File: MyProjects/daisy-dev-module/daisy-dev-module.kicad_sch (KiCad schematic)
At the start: 28 parts, among them J13 Gate_1, J14 Gate_2, J17 Gate_OUT_1, J18 Gate_OUT_2, Q1 MMBT3904, Q2 MMBT3904, U8 TL074

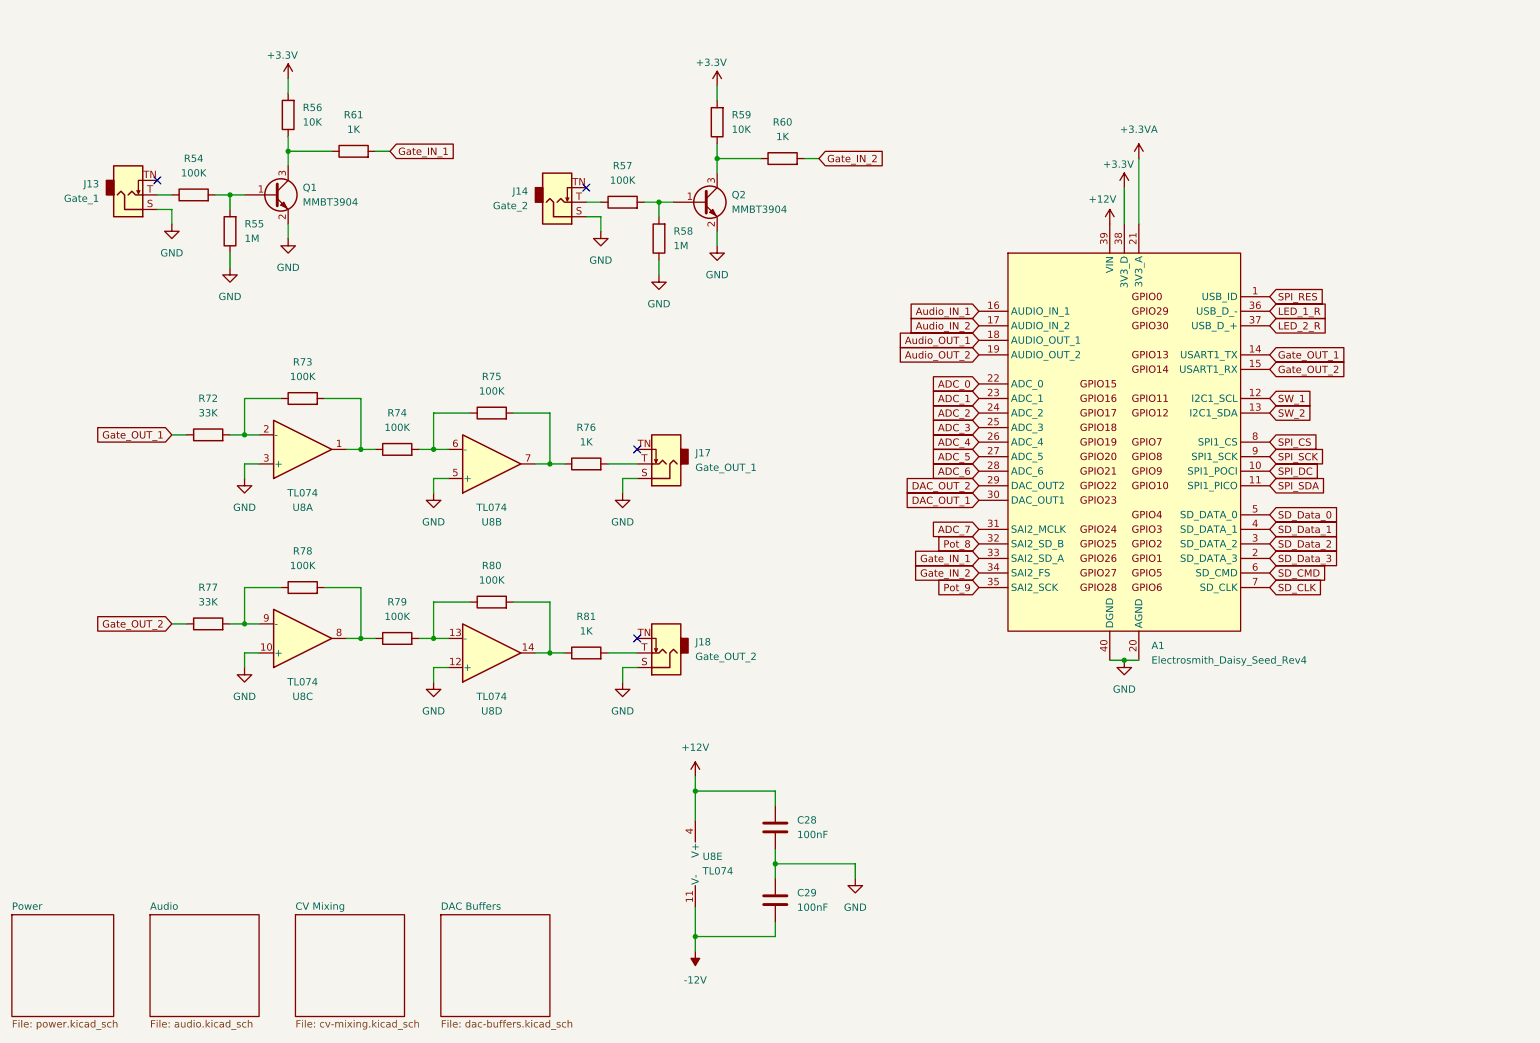
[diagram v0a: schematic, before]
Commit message: Create daisy-dev-module-test repo
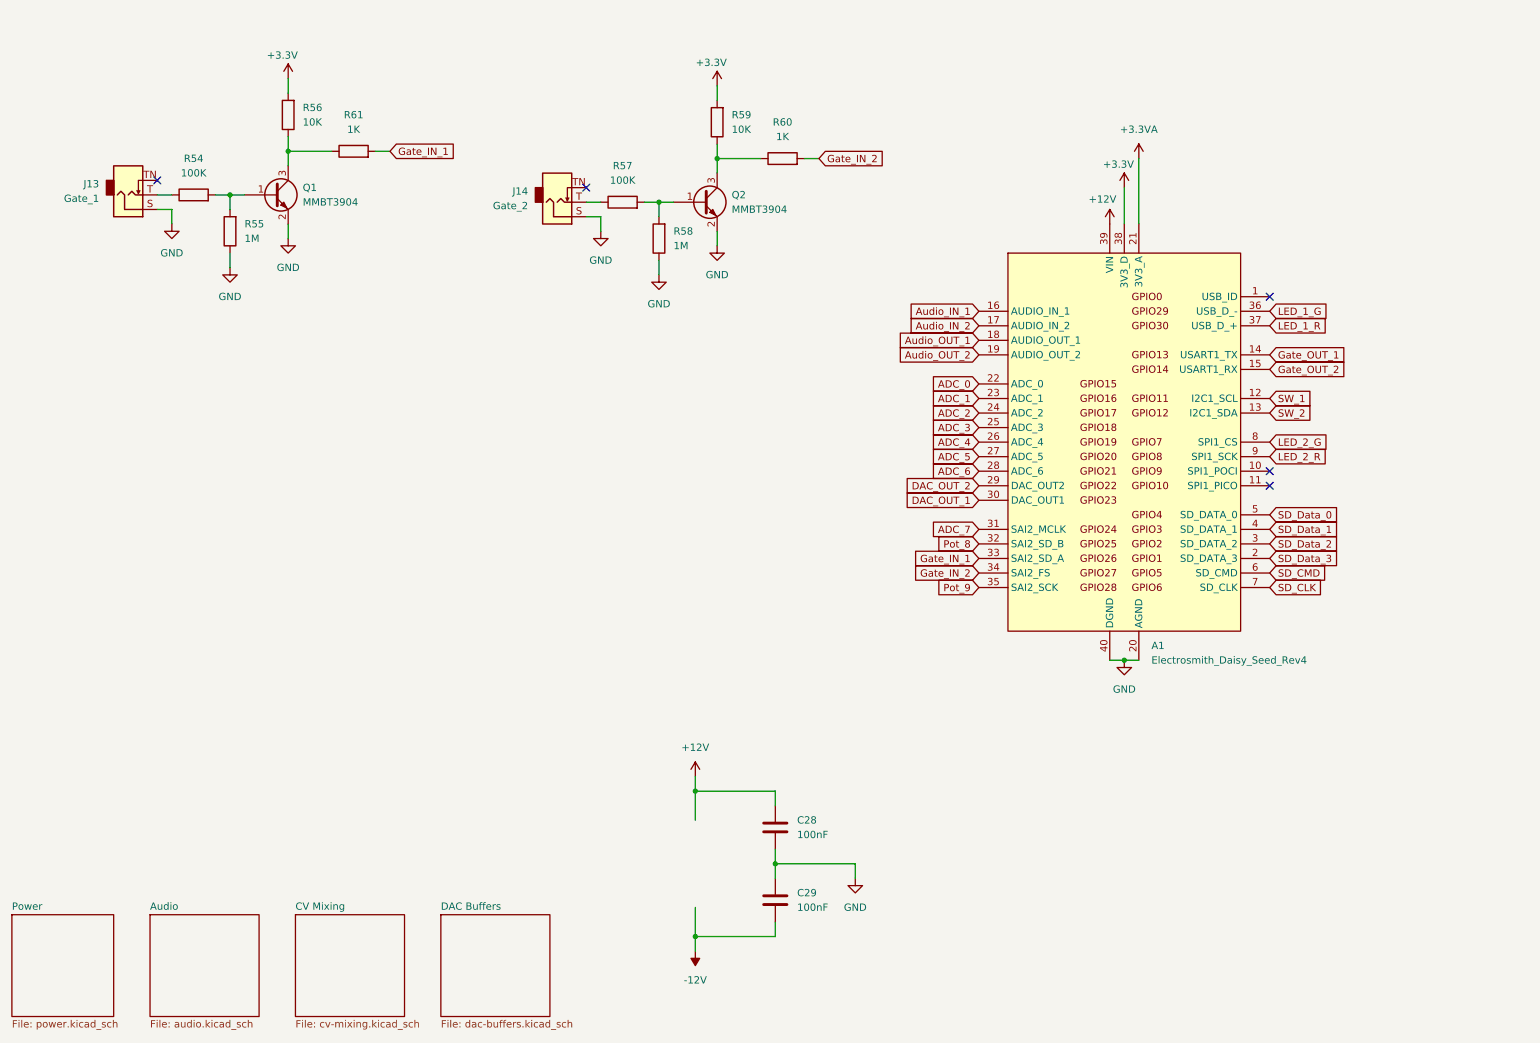
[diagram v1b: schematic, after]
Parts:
- removed J17: Gate_OUT_1, Connector_Audio:Jack_3.5mm_QingPu_WQP-PJ398SM_Vertical_CircularHoles, symbol Connector_Audio:AudioJack2_SwitchT
- removed J18: Gate_OUT_2, Connector_Audio:Jack_3.5mm_QingPu_WQP-PJ398SM_Vertical_CircularHoles, symbol Connector_Audio:AudioJack2_SwitchT
- removed R72, R77: 33K, Resistor_SMD:R_0805_2012Metric_Pad1.20x1.40mm_HandSolder, symbol Device:R
- removed R73, R74, R75, R78, R79, R80: 100K, Resistor_SMD:R_0805_2012Metric_Pad1.20x1.40mm_HandSolder, symbol Device:R
- removed R76, R81: 1K, Resistor_SMD:R_0805_2012Metric_Pad1.20x1.40mm_HandSolder, symbol Device:R
- removed U8: TL074, Package_SO:SOIC-14_3.9x8.7mm_P1.27mm, symbol Amplifier_Operational:TL074
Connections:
- net SPI_SCK is gone; now on net LED_2_R: A1.9 (SPI1_SCK)
- net LED_1_R: now also A1.37 (USB_D_+); no longer A1.36 (USB_D_-)
- net LED_2_R: no longer A1.37 (USB_D_+)
- net SPI_CS renamed LED_2_G
- net SPI_DC: no longer names the net of A1.10 (SPI1_POCI)
- net SPI_RES: no longer names the net of A1.1 (USB_ID)
- net SPI_SDA: no longer names the net of A1.11 (SPI1_PICO)
- new net LED_1_G: A1.36 (USB_D_-)
- no-connect marks 4 -> 5

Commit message: Update delay-module.cpp
Add encoder (does nothing right now) and remove one LED.
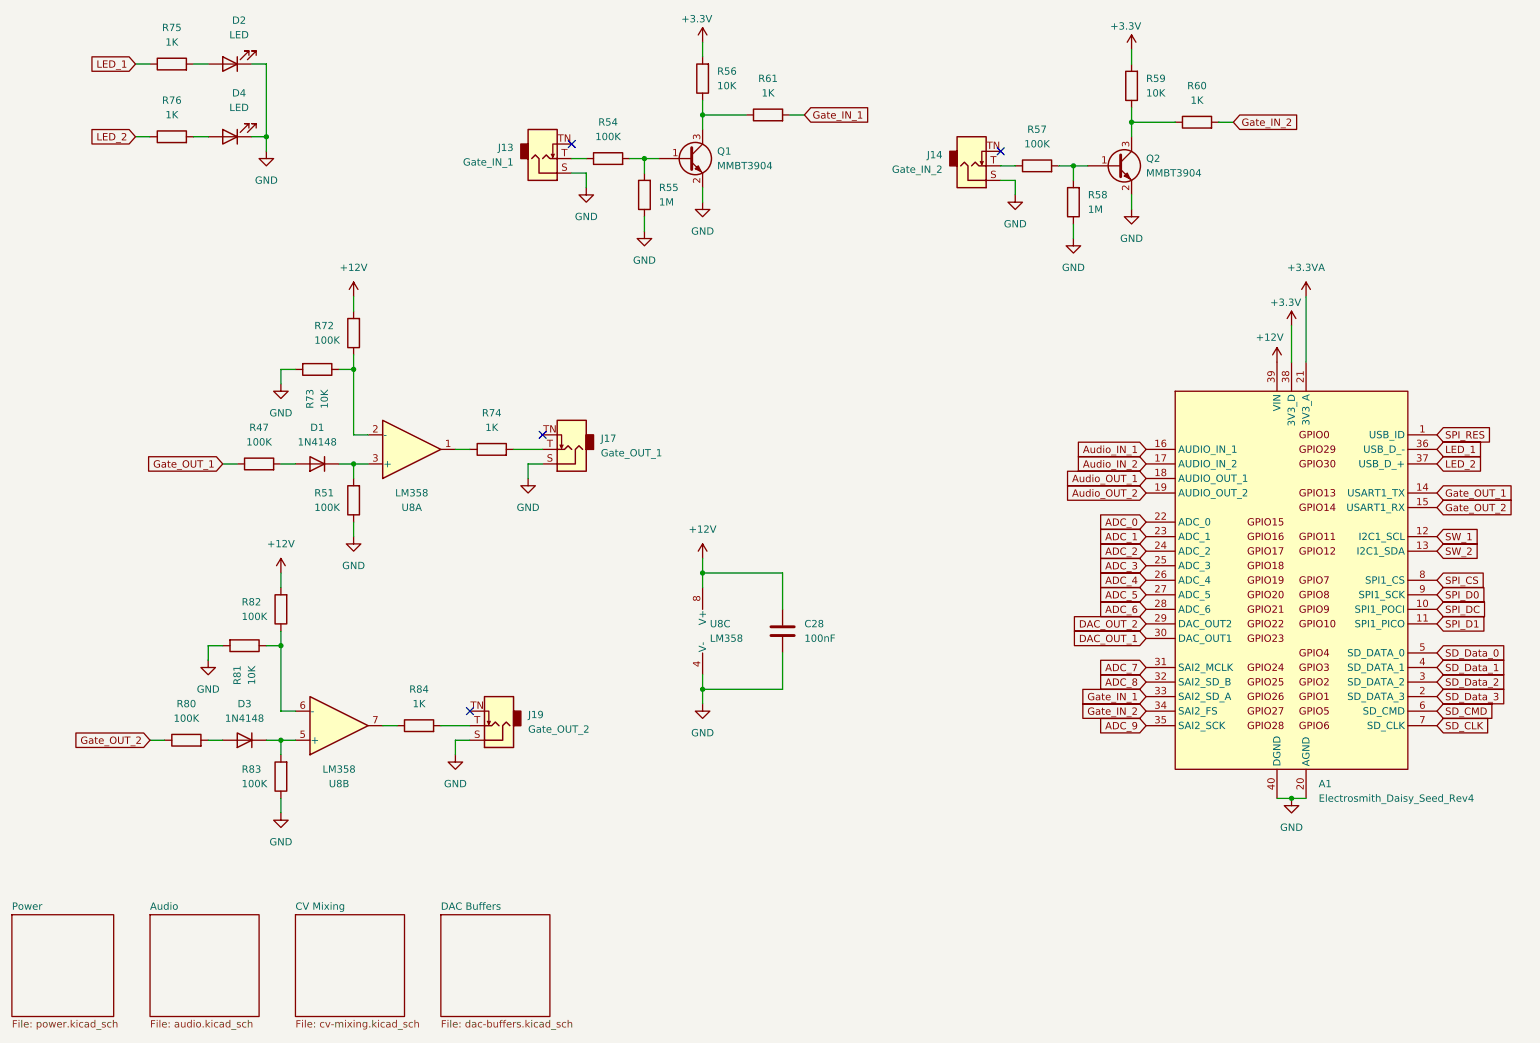
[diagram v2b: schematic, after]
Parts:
- removed C29: 100nF, Capacitor_SMD:C_0805_2012Metric_Pad1.18x1.45mm_HandSolder, symbol Device:C
- added D1, D3: 1N4148, Diode_THT:D_DO-35_SOD27_P7.62mm_Horizontal, symbol Diode:1N4148
- added D2: LED, LED_THT:LED_D3.0mm, symbol Device:LED
- added D4: LED, symbol Device:LED
- added J17: Gate_OUT_1, Connector_Audio:Jack_3.5mm_QingPu_WQP-PJ398SM_Vertical_CircularHoles, symbol Connector_Audio:AudioJack2_SwitchT
- added J19: Gate_OUT_2, Connector_Audio:Jack_3.5mm_QingPu_WQP-PJ398SM_Vertical_CircularHoles, symbol Connector_Audio:AudioJack2_SwitchT
- added R47, R51, R72, R80, R82, R83: 100K, Resistor_SMD:R_0805_2012Metric_Pad1.20x1.40mm_HandSolder, symbol Device:R
- added R73, R81: 10K, Resistor_SMD:R_0805_2012Metric_Pad1.20x1.40mm_HandSolder, symbol Device:R
- added R74, R75, R76, R84: 1K, Resistor_SMD:R_0805_2012Metric_Pad1.20x1.40mm_HandSolder, symbol Device:R
- added U8: LM358, Package_DIP:DIP-8_W7.62mm_Socket_LongPads, symbol Amplifier_Operational:LM358
- J13: value Gate_1 -> Gate_IN_1
- J14: value Gate_2 -> Gate_IN_2
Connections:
- net +12V: now also R72.2, R82.2, U8.8 (V+)
- net GND: now also D2.1 (K), D4.1 (K), J17.S, J19.S, R51.1, R73.2, R81.2, R83.1, U8.4 (V-)
- net Gate_OUT_1: now also R47.1
- net Gate_OUT_2: now also R80.1
- net SPI_RES: now reaches A1.1 (USB_ID)
- net SPI_DC: now reaches A1.10 (SPI1_POCI)
- net SPI_D1: now reaches A1.11 (SPI1_PICO)
- net LED_1_G renamed LED_1
- net LED_1: now also R75.1
- net LED_1_R renamed LED_2
- net LED_2: now also R76.1
- net LED_2_G renamed SPI_CS
- net LED_2_R renamed SPI_D0
- net Pot_8 renamed ADC_8
- net Pot_9 renamed ADC_9
- new net: D4.2 (A), R76.2
- new net: D3.2 (A), R80.2
- new net: R81.1, R82.1, U8.6 (-)
- new net: J19.T, R84.2
- new net: D1.1 (K), R51.2, U8.3 (+)
- new net: D1.2 (A), R47.2
- new net: D2.2 (A), R75.2
- new net: D3.1 (K), R83.2, U8.5 (+)
- new net: R84.1, U8.7
- new net: R72.1, R73.1, U8.2 (-)
- new net: R74.1, U8.1
- new net: J17.T, R74.2
- no-connect marks 5 -> 4
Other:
- moved on the sheet: A1, C28, J13, J14, Q1, Q2, R54, R55, R56, R57, R58, R59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
